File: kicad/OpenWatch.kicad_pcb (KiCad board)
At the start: 4 copper layers, 79 parts, among them J1 USB_microB_2040002-1, J3 Conn_02x05_Odd_Even, J4 Vibration Motor, J6 Conn_01x05, Q1 RUM002N02T2L, Q2 RUM002N02T2L, Q3 RUM002N02T2L, SW1 SW_Push, SW2 SW_Push, U1 STM32F303RCT6-48, U2 TPS2113ADRBR, U3 TSP70933DBVR, U4 MCP73831T-2ACI, U5 AT42QT1070-MMHR, U6 TPS60241DGKR, U7 RT9818A-18GV, U8 WM1389CT-ND, U9 LSM6DSL, Y1 ECS.327, Y2 FA-238

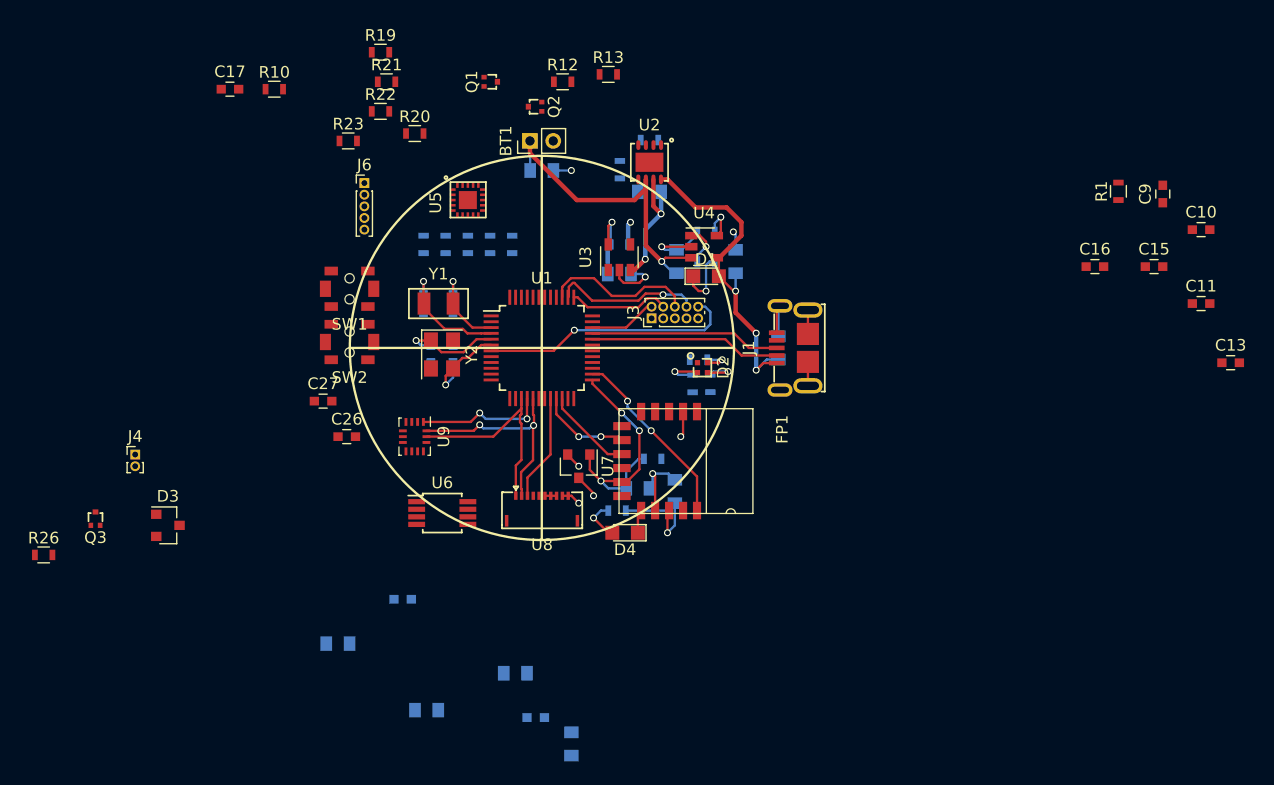
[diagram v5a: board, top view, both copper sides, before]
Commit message: Finish majority of routing
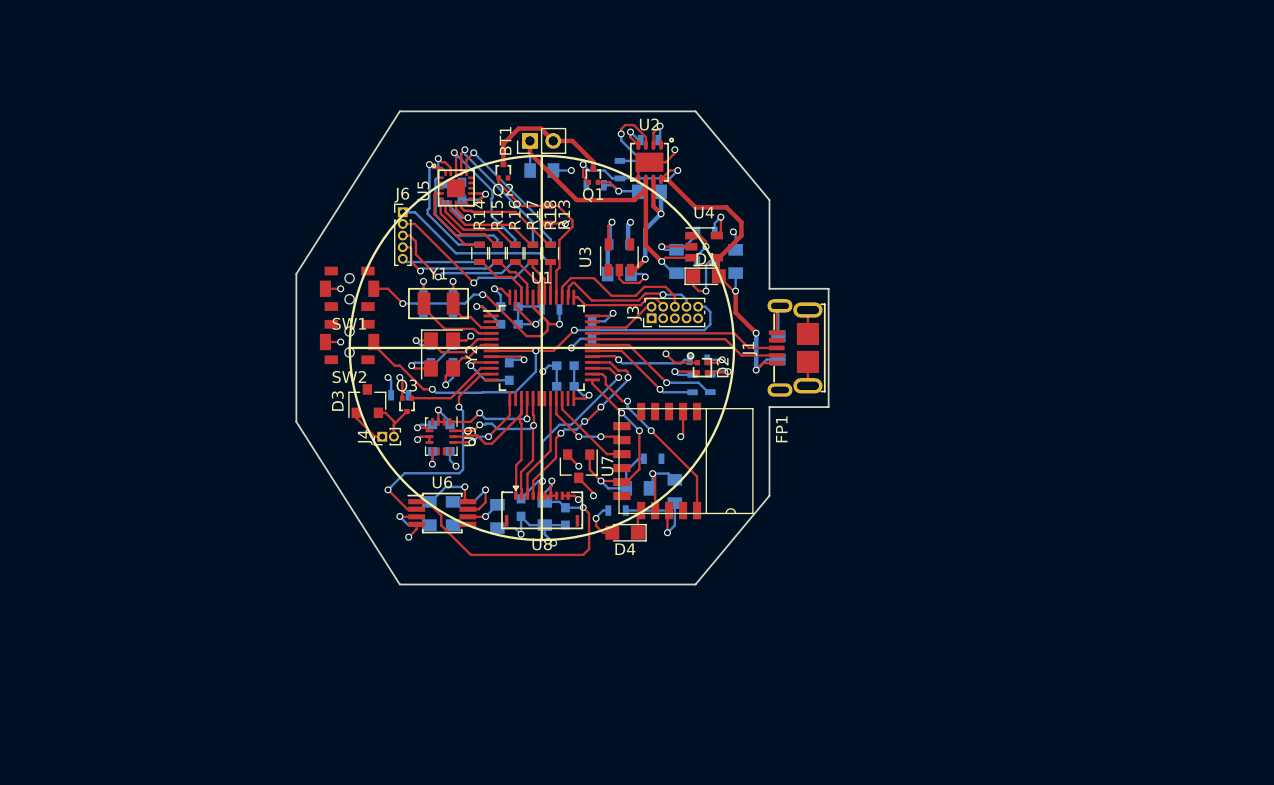
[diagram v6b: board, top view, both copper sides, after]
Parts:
- C10, C11, C13, C15, C16, C17, C26, C27, C9, R1, R10, R12, R19, R20, R21, R22, R23, R26: moved to B.Cu
- R14, R15, R16, R17, R18: moved to F.Cu
- moved C11 59.4 mm to (56.9, 79.2)
- moved C13 57.1 mm to (61.7, 82.8), turned to 180 degrees
- moved C15 56.1 mm to (56.9, 83.3), turned to 90 degrees
- moved C9 53.9 mm to (61.7, 84.6), turned to 180 degrees
- moved C10 53.0 mm to (64.0, 79.7), turned to 270 degrees
- moved C16 50.4 mm to (56.9, 77.7)
- moved R1 49.8 mm to (60.5, 78.0), turned to 180 degrees
- moved R26 33.5 mm to (47.5, 85.3), turned to 180 degrees
- moved Q3 28.1 mm to (48.1, 86.7), turned to 180 degrees
- moved C20 23.2 mm to (50.0, 95.5), turned to 270 degrees
- moved R19 22.6 mm to (60.5, 73.2), turned to 90 degrees
- moved C17 21.8 mm to (52.8, 67.8), turned to 90 degrees
- moved J4 21.3 mm to (46.0, 88.9), turned to 90 degrees
- moved D3 20.2 mm to (44.7, 85.9), turned to 90 degrees
- moved R21 18.4 mm to (57.4, 73.2), turned to 90 degrees
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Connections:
- U1 pad 12: /BATT_EN -> Net-(U1-Pad12)
- U1 pad 40: Net-(U1-Pad40) -> /BATT_EN
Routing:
- net GND: track 35.6 -> 99.7 mm, vias 8 -> 27
- net +3V3: track 13.3 -> 58.3 mm, vias 3 -> 14
- net +5V: track 1.00 -> 29.1 mm, vias 0 -> 2
- net Net-(R1-Pad1): track 0.00 -> 25.0 mm, vias 0 -> 3
- net /5V_EN: track 0.00 -> 20.3 mm, vias 0 -> 2
- net /DISP_EN: track 0.00 -> 18.6 mm, vias 0 -> 2
- net /STM_NRST: track 22.1 -> 40.5 mm, vias 1 -> 3
- net /EXTCOMIN: track 0.00 -> 18.1 mm, vias 0 -> 4
- net /BATT_EN: track 0.00 -> 15.3 mm
- net /KEY_0: track 0.00 -> 14.5 mm
- net /KEY_1: track 0.00 -> 14.0 mm, vias 0 -> 1
- net Net-(R22-Pad2): track 0.00 -> 13.4 mm, vias 0 -> 1
- net Net-(R20-Pad2): track 0.00 -> 12.7 mm, vias 0 -> 1
- net Net-(R19-Pad2): track 0.00 -> 12.6 mm, vias 0 -> 1
- net /VUSB: track 29.5 -> 41.8 mm, vias 3 -> 5
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- added copper zone on In1.Cu, net +3V3
- added copper zone on In2.Cu, net GND
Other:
- board outline added: 45.7 x 40.6 mm

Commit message: Finish PCB routing
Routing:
- net GND: track 99.7 -> 121.9 mm, vias 27 -> 32
- net /IMU_INT_2: track 0.00 -> 16.3 mm, vias 0 -> 2
- net /IMU_INT_1: track 0.00 -> 14.1 mm, vias 0 -> 2
- net +3V3: track 58.3 -> 69.5 mm, vias 14 -> 16
- net Net-(C7-Pad1): track 11.2 -> 15.4 mm
- net Net-(C19-Pad2): track 0.00 -> 3.16 mm, vias 0 -> 1
- net /STM_NRST: track 40.5 -> 43.1 mm
- net /MOTOR_EN: track 7.89 -> 10.4 mm, vias 0 -> 1
- net /VUSB: track 41.8 -> 44.2 mm, vias 5 -> 6
- net Net-(R21-Pad2): track 12.0 -> 12.5 mm
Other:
- net class Default: clearance 0.2 -> 0.1016
- rule trace_clearance: 0.2 -> 0.1016
